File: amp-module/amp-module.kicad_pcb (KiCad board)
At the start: 2 copper layers, 80 x 22 mm, 29 parts, among them IC1 AD5245BRJZ10-RL7, U5 TPA3221DDVR

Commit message: finish everything
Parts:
- removed R7: 10kΩ, Resistor_SMD:R_0603_1608Metric_Pad0.98x0.95mm_HandSolder
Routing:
- net Net-(U1-AGP4): track 49.2 -> 45.8 mm
- net Net-(U5-OUT1_P): track 14.9 -> 15.4 mm
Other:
- board text removed: "A: 1110"

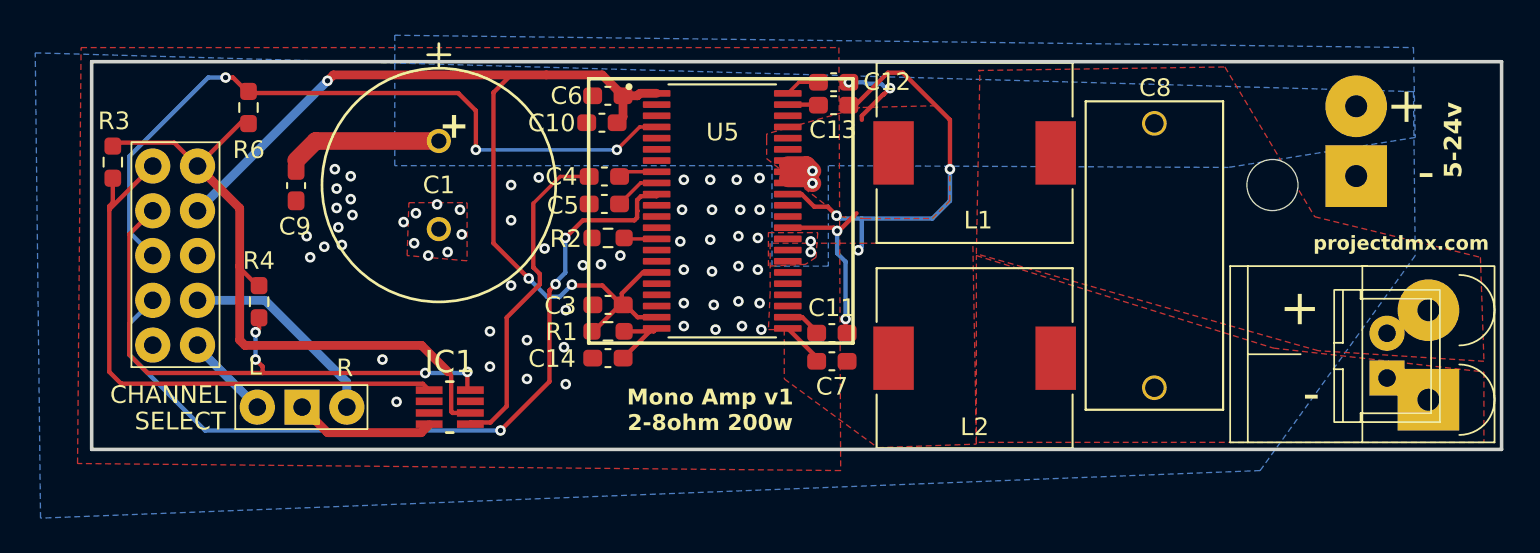
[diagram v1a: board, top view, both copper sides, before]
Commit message: replace amp with screw pot
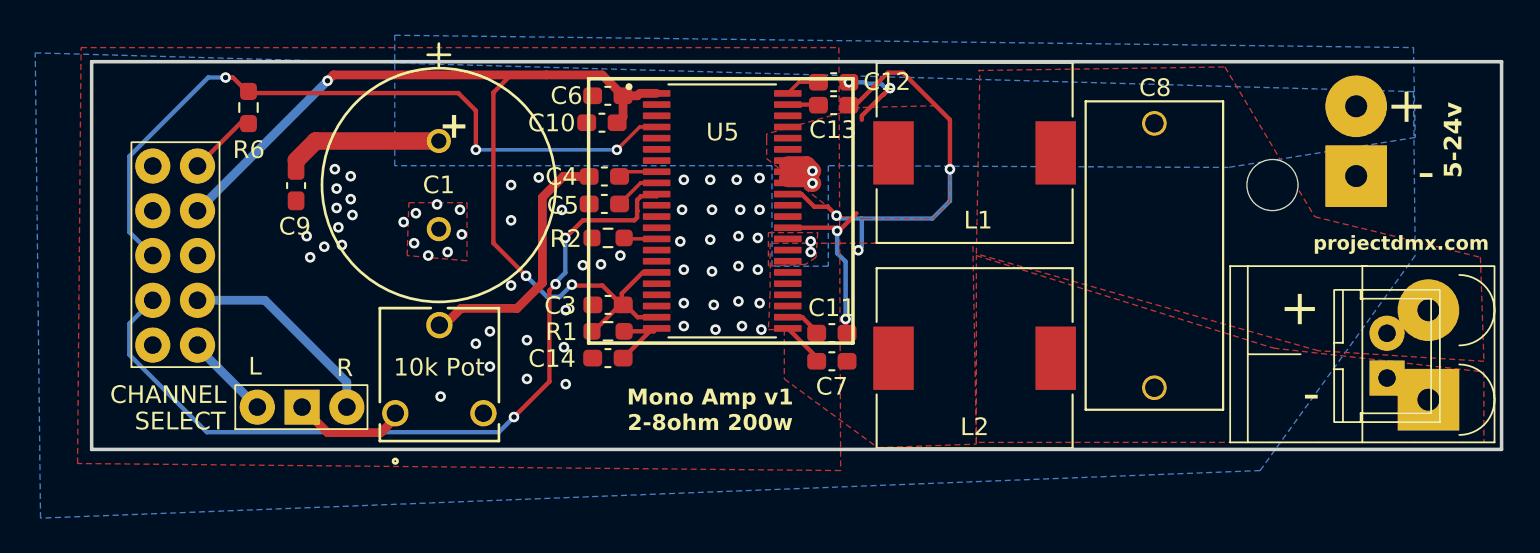
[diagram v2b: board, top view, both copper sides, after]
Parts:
- removed IC1: AD5245BRJZ10-RL7, Imported:SOT65P280X145-8N
- removed R3, R4: 4.7kΩ, Resistor_SMD:R_0603_1608Metric_Pad0.98x0.95mm_HandSolder
- added REF**: 601030_AVX, Imported:601030_AVX, F.Cu at (134.4, 95.9)
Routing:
- net 3V3: track 37.7 -> 3.93 mm
- net Net-(U1-GP1): track 33.3 -> 0.00 mm
- net Net-(U1-GP2): track 32.6 -> 0.00 mm, vias 4 -> 0
- net Net-(IC1-W): track 18.8 -> 14.8 mm
- net Net-(IC1-A): track 8.00 -> 6.51 mm
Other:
- board text added: "10k Pot"
